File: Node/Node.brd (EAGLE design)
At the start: 160 x 100 mm, 28 parts, among them IC1 4050D, IC2 LP298XS, IC3 DS3231/SO, M2 WIRELESS-NRF24L01-PA-EXT, U2 ATMEGA328P-PU, X1 MICROSD

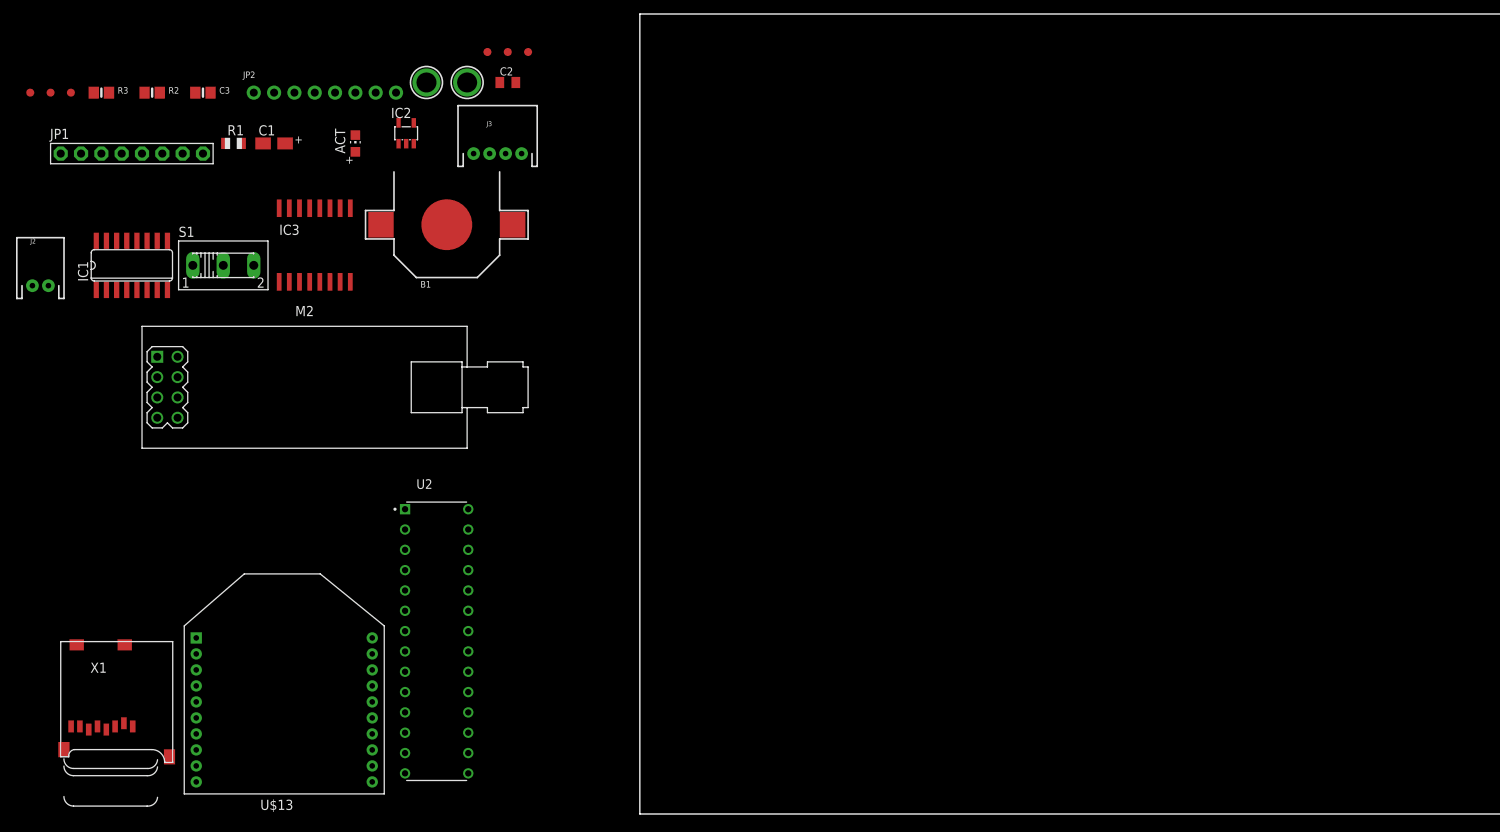
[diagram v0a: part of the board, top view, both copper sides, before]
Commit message: Added some connections to Node schematic
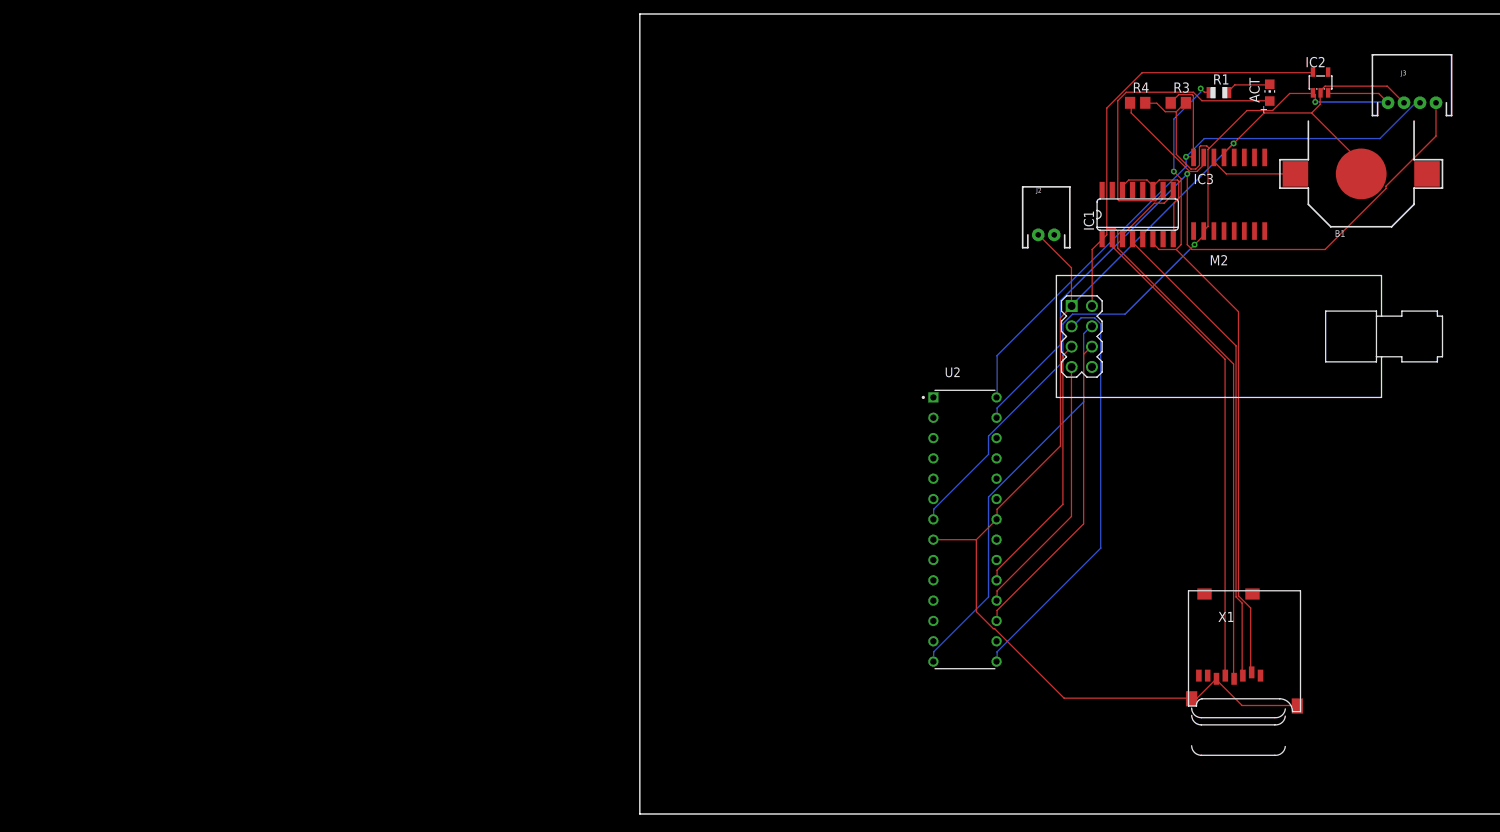
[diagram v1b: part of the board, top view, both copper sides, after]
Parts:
- removed C1: 10uF/10V, adafruit:A/3216-18R
- removed C2: 0.1uF, adafruit:C0805K
- removed C3: 1uF, microbuilder:0805-NO
- removed FID1, FID2, FID3, FID4: FIDUCIAL"", microbuilder:FIDUCIAL_1MM
- removed JP1: (no value), adafruit:1X08-BIG
- removed JP2: (no value), microbuilder:1X08_ROUND_70
- removed R2: 10K, microbuilder:0805-NO
- removed S1: (no value), switch:255SB
- removed U$1, U$2: FIDUCIAL, adafruit:FIDUCIAL_1MM
- removed U$13: XBEE, adafruit:XBEE
- removed U$7, U$8: MOUNTINGHOLE2.5, microbuilder:MOUNTINGHOLE_2.5_PLATED
- added R4: (no value), rcl:R0805
- R3: value 10K -> (none); device microbuilder:0805-NO -> rcl:R0805
- moved X1 141.1 mm to (68.6, 27.9)
- moved R3 134.6 mm to (67.3, 88.9)
- moved J2 125.9 mm to (50.8, 72.4)
- moved IC1 125.9 mm to (62.2, 74.9)
- moved R1 123.4 mm to (72.4, 90.2)
- moved IC2 114.5 mm to (85.1, 91.4)
- moved ACT 114.5 mm to (78.7, 90.2)
- moved B1 114.5 mm to (90.2, 80.0)
- moved IC3 114.5 mm to (73.7, 77.5)
- moved J3 114.5 mm to (96.5, 88.9)
- moved M2 114.5 mm to (72.4, 59.7)
- moved U2 67.5 mm to (40.6, 35.6)
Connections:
- removed net 3.3V: C3.2, IC3.2, JP2.1, R2.1, R3.1
- removed net GND_RTC: B1.-, C3.1, IC3.13, JP2.2
- removed net VCC_SD: C2.1, IC2.1, IC2.3, JP1.1, M2.2, U2.7
- new net +5V: IC2.1, IC2.3, IC3.2, J3.1, R3.2, R4.2, U2.7
- new net CE: M2.3, U2.15
- new net CSN: M2.4, U2.14
- new net GND: B1.-, IC2.2, IC3.13, J2.1, J3.2, M2.1, U2.22, U2.8, X1.6, X1.MT1, X1.MT2
- new net MISO: M2.7, U2.18
- new net MOSI: M2.6, U2.17
- new net SCK: M2.5, U2.19
- new net V_EXTERNAL_BATTERY: J2.2
- net !RTC_RST: no longer JP2.8
- net +3V3: now also M2.2; no longer C1.+, JP1.2
- net 32KHZ: no longer JP2.6
- net CD: no longer JP1.8
- net CLK: no longer JP1.4
- net CS: no longer JP1.7
- net DI: no longer JP1.6
- net DO: no longer JP1.5
- net GND_SD: no longer C1.-, C2.2, IC2.2, JP1.3, M2.1, U2.22, U2.8, X1.6, X1.MT1, X1.MT2
- net SCL: now also J3.3, R3.1, U2.28; no longer JP2.3, R2.2
- net SDA: now also J3.4, R4.1, U2.27; no longer JP2.4, R3.2
- net SQW: no longer JP2.7
- net VBAT: no longer JP2.5
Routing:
- net GND: track 0.00 -> 173.6 mm, vias 0 -> 1
- net +5V: track 0.00 -> 117.7 mm, vias 0 -> 2
- net +3V3: track 0.00 -> 116.7 mm
- net SDA: track 0.00 -> 105.9 mm, vias 0 -> 1
- net N$3: track 0.00 -> 84.1 mm, vias 0 -> 2
- net SCL: track 0.00 -> 83.9 mm, vias 0 -> 1
- net N$2: track 0.00 -> 60.4 mm
- net N$5: track 0.00 -> 60.3 mm
- net CE: track 0.00 -> 52.0 mm
- net CSN: track 0.00 -> 50.2 mm
- net MOSI: track 0.00 -> 39.3 mm
- net N$1: track 0.00 -> 38.7 mm
- net MISO: track 0.00 -> 33.1 mm
- net SCK: track 0.00 -> 33.1 mm
- net GND_SD: track 0.00 -> 17.0 mm
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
